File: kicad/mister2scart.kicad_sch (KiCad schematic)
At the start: 11 parts, among them J1 SCART-F, J2 DE15-F, J3 SJ1-3523NG, J4 RCA-F, SW2 SS12D10G6-WJ, U1 MAX662ACPA

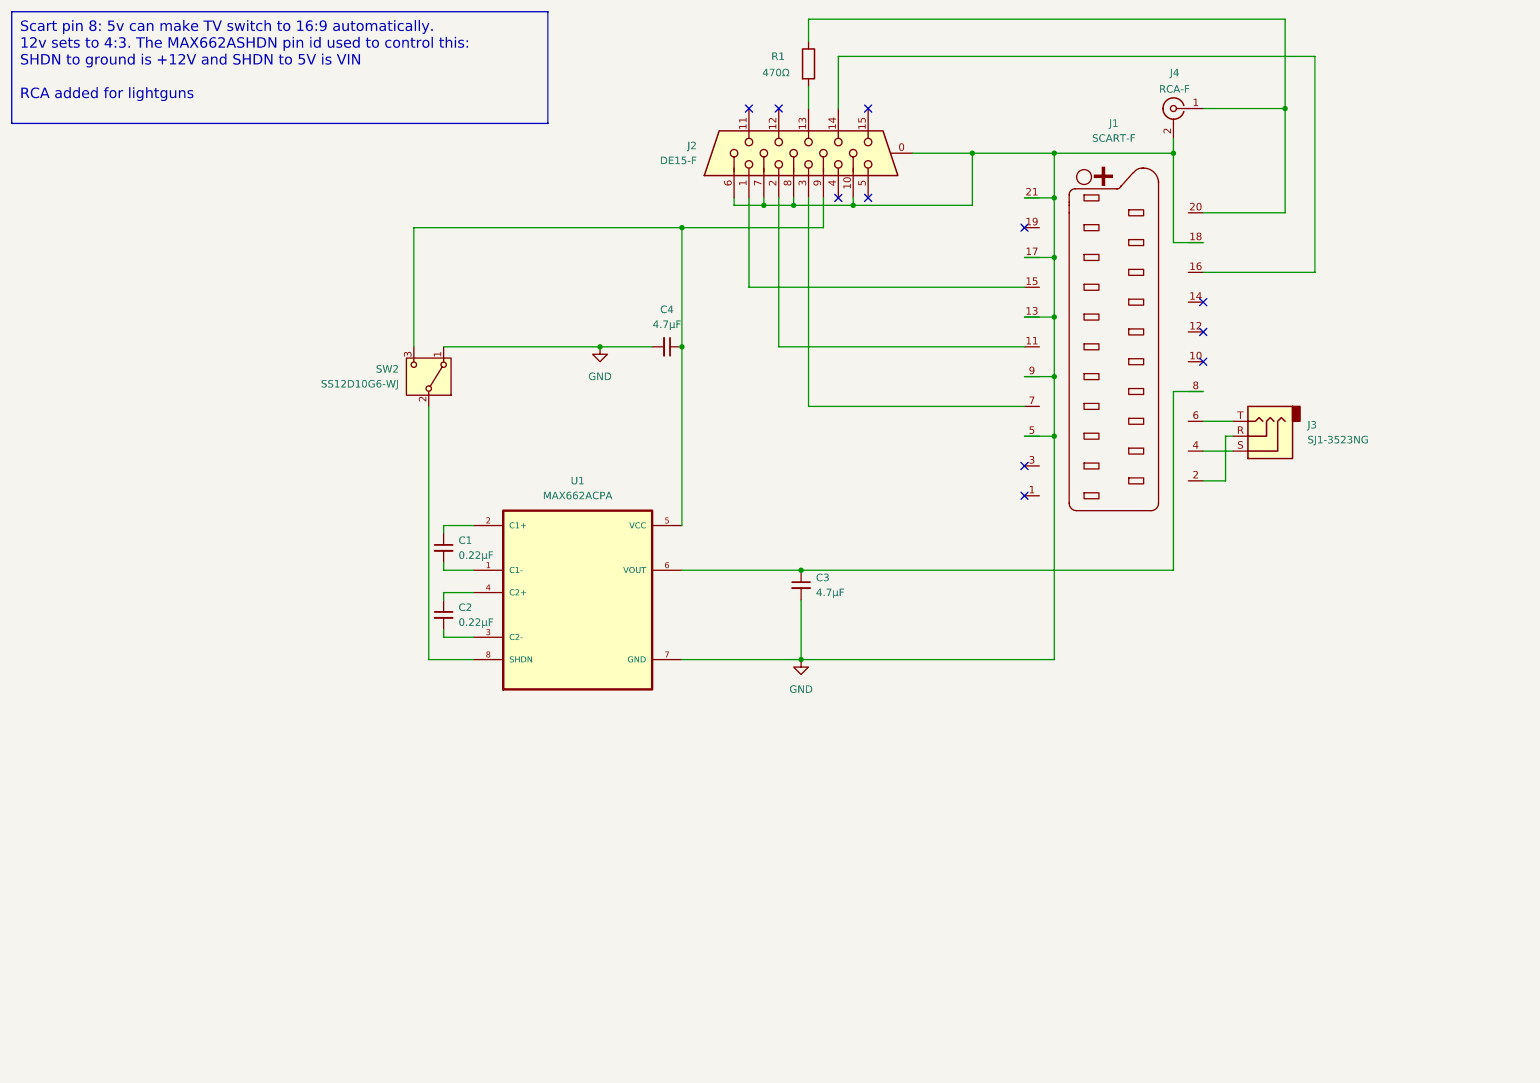
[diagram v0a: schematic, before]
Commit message: V0.2:
- Corrected pinout of the SCART connection, as SCART to SCART cables have some pins crossed.
- Marked polarity in the silkscreen for polarized capacitors
- Increase footprint for resistor
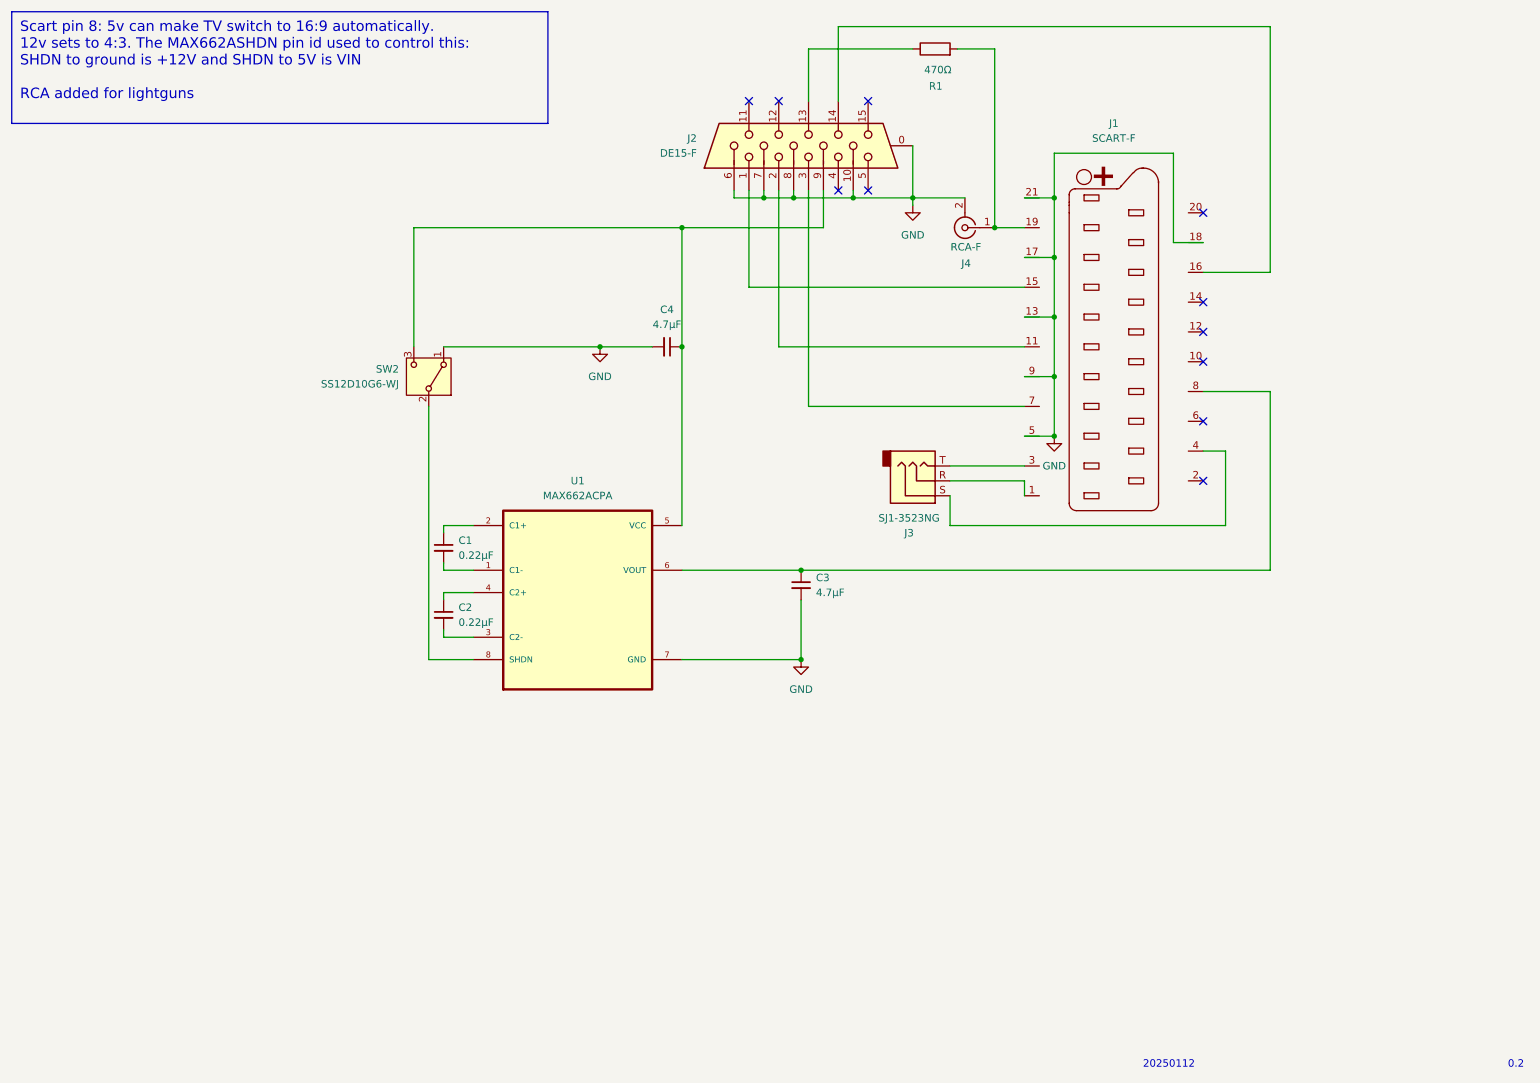
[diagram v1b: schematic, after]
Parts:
- R1: footprint Resistor_THT:R_Axial_DIN0207_L6.3mm_D2.5mm_P7.62mm_Horizontal -> Resistor_THT:R_Axial_DIN0207_L6.3mm_D2.5mm_P10.16mm_Horizontal
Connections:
- net at J2.13: now also R1.1; no longer R1.2
- net at J1.1 (P1): now also J3.R
- net at J1.19 (P19): now also J4.1 (In), R1.2
- net at J1.2 (P2): no longer J3.R
- net at J1.3 (P3): now also J3.T
- net at J1.6 (P6): no longer J3.T
- now unconnected: J1.20 (P20)
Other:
- note added: "0.2"
- note added: "20250112"
- moved on the sheet: J2, J3, J4, R1

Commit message: v0.3: fixed sync connector pinout
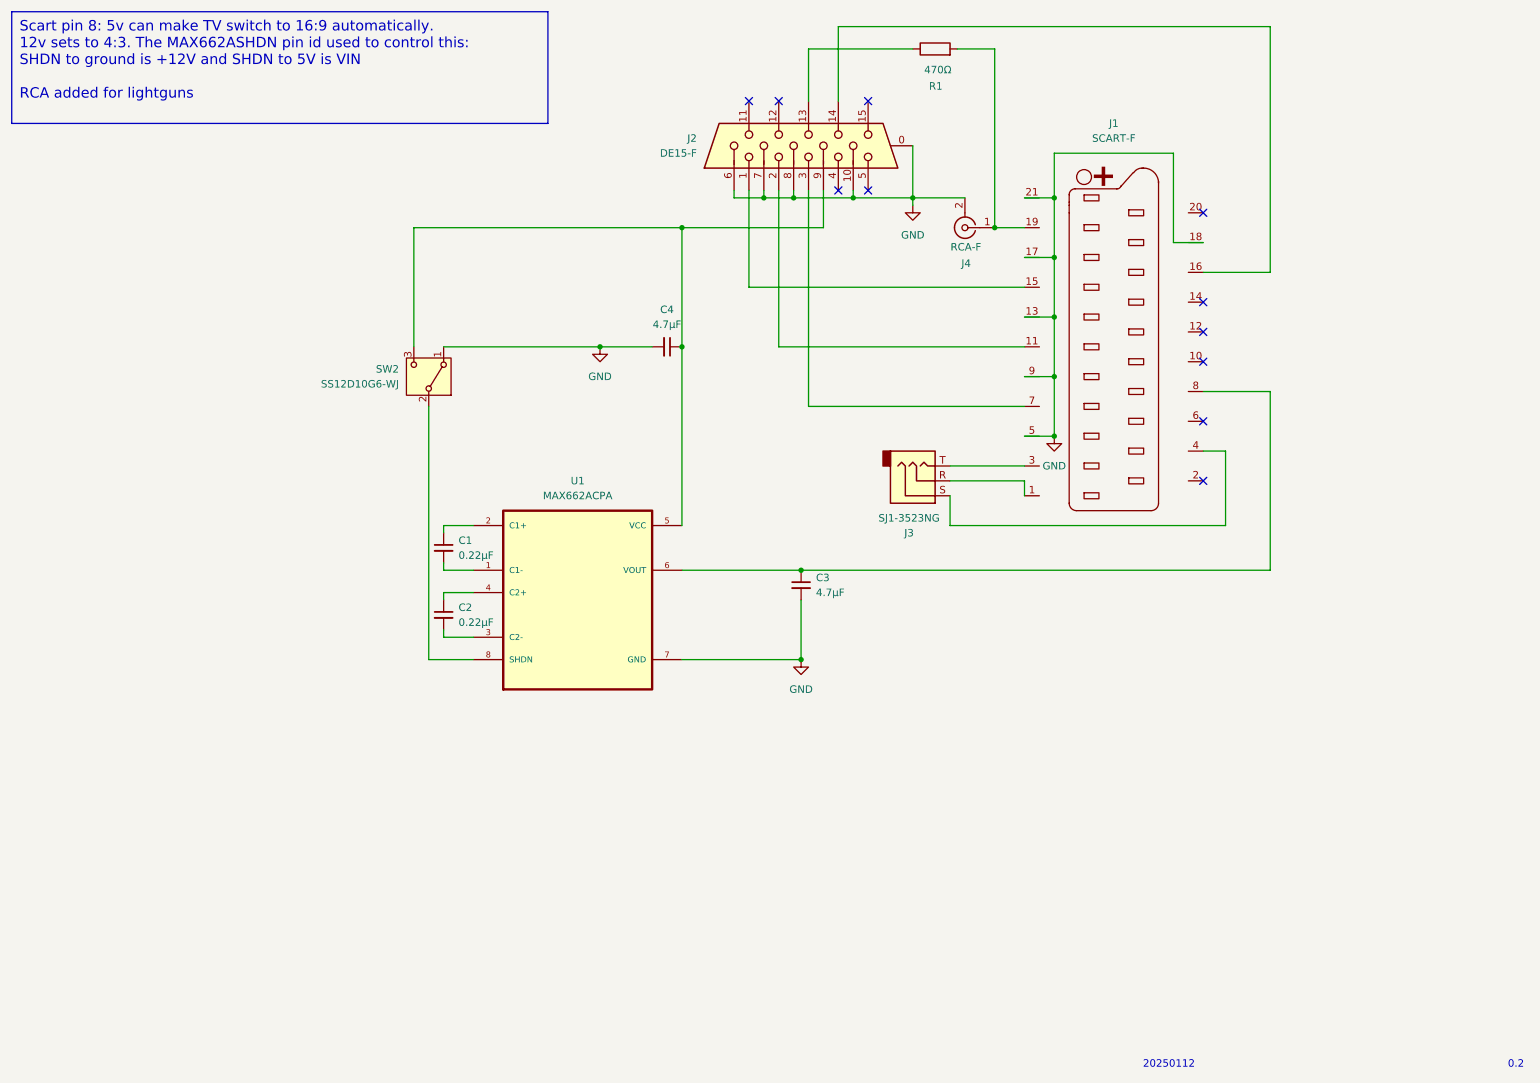
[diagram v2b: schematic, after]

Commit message: Include schematic PDF
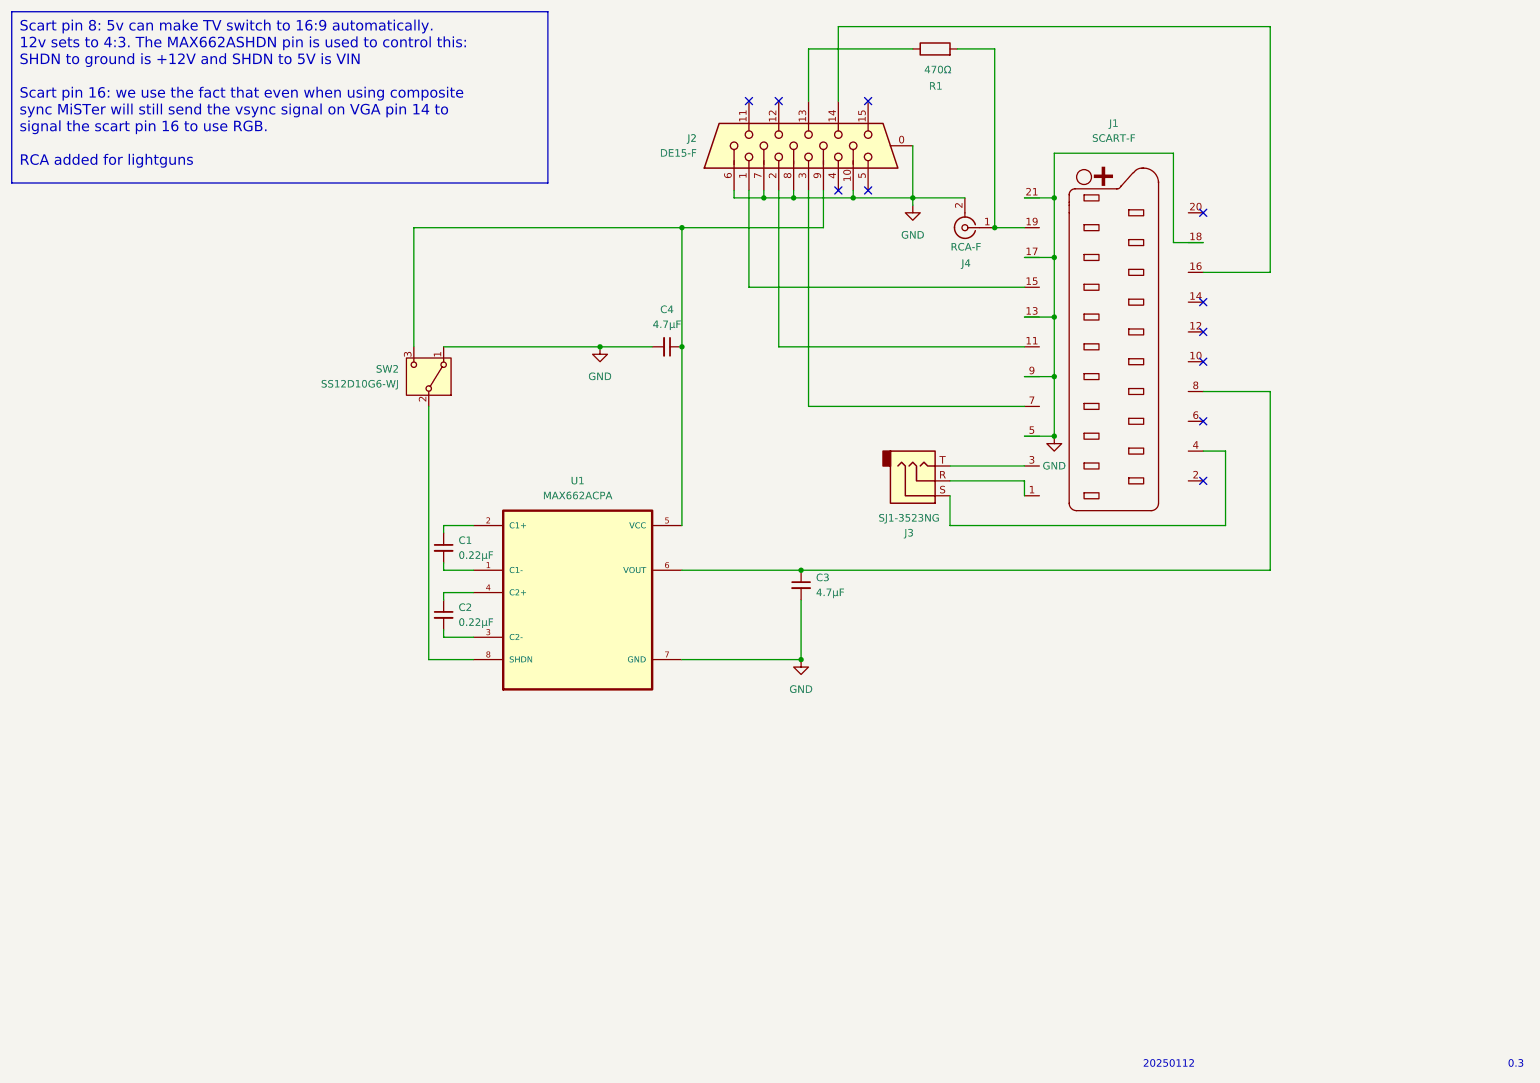
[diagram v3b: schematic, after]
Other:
- note added: "0.3"
- note removed: "0.2"
- title: (none) -> MiSTer2SCART
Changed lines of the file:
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@@
 	(generator_version "9.0")
 	(paper "A4")
+	(title_block
+		(title "MiSTer2SCART")
+		(comment 1 "https://github.com/madmalkav/mister2scart")
+	)
 	(text "20250112"
 		(exclude_from_sim no)
@@
 		)
 	)
-	(text "0.2"
+	(text "0.3"
 		(exclude_from_sim no)
 		(at 270.51 193.548 0)
@@
 		)
 	)
-	(text_box "Scart pin 8: 5v can make TV switch to 16:9 automatically.\n12v sets to 4:3. The MAX662ASHDN pin id used to control this:\nSHDN to ground is +12V and SHDN to 5V is VIN\n\nRCA added for lightguns"
+	(text_box "Scart pin 8: 5v can make TV switch to 16:9 automatically.\n12v sets to 4:3. The MAX662ASHDN pin is used to control this:\nSHDN to ground is +12V and SHDN to 5V is VIN\n\nScart pin 16: we use the fact that even when using composite\nsync MiSTer will still send the vsync signal on VGA pin 14 to \nsignal the scart pin 16 to use RGB.\n\nRCA added for lightguns"
 		(exclude_from_sim no)
 		(at 13.97 13.97 0)
-		(size 91.44 19.05)
+		(size 91.44 29.21)
 		(margins 1.3335 1.3335 1.3335 1.3335)
 		(stroke
 			(width 0)
-			(type default)
+			(type solid)
 		)
 		(fill
